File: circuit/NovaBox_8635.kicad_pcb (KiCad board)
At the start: 2 copper layers, 82 x 30 mm, 87 parts, among them P1 MH, P2 MH, P3 MH, P4 MH, P5 USB, Q1 MMBT3904, Q2 IRLML6344, Q3 IRLML6401, Q4 MMBT3904, Q5 MMBT3904, SW1 PIO18, SW2 PIO21, SW3 PIO8, SW4 PIO0, SW5 PIO1, SW6 ON/OFF, U1 MCP6004, U2 CSR8635_MODULE, U3 CSR_DebugSmall, U4 PAM8304, U5 PAM8304, U6 LT1308

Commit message: first draft of PCB; deleted footprints
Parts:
- removed D9: PWR, NovaBox:LED_0805
- removed R5: 1K, NovaBox:R_0805
- moved R1 10.7 mm to (118.9, 63.8)
- moved R3 9.97 mm to (120.7, 57.4), turned to 90 degrees
- moved Q3 9.54 mm to (117.6, 57.9), turned to 0 degrees
- moved Q5 8.93 mm to (115.6, 61.9)
- moved C3 7.71 mm to (116.8, 65.8)
- moved R2 7.70 mm to (114.8, 65.8)
- moved C1 2.03 mm to (110.8, 60.7)
- moved R6 2.03 mm to (110.8, 62.7)
- moved R9 1.13 mm to (110.8, 66.8)
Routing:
- net VR_SHDN: track 5.71 -> 22.7 mm
- net Net-(R9-Pad2): track 134.6 -> 126.0 mm
- net +BATT: track 162.5 -> 168.0 mm
- net +5V: track 129.2 -> 123.9 mm
- net 1V8: track 18.2 -> 14.3 mm
- net Net-(D9-Pad1): track 2.05 -> 0.00 mm
- net Net-(Q3-Pad1): track 5.13 -> 6.81 mm
- net Net-(BT1-Pad2): track 81.1 -> 80.1 mm
- net Net-(D1-Pad3): track 5.81 -> 6.55 mm
- net LED2: track 8.97 -> 9.62 mm

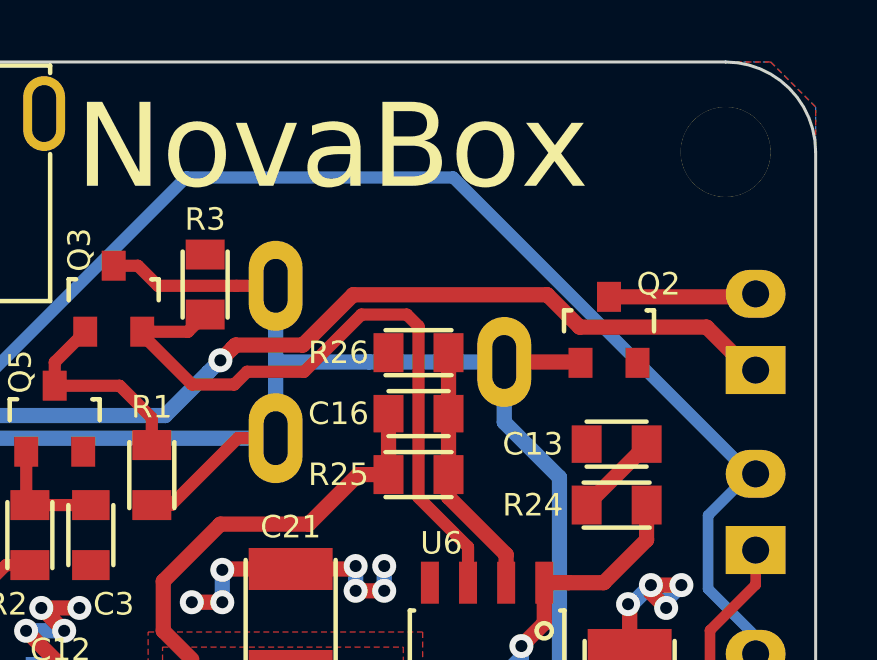
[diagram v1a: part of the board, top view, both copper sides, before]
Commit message: added OSHW; fixed trace over zone; fixed date
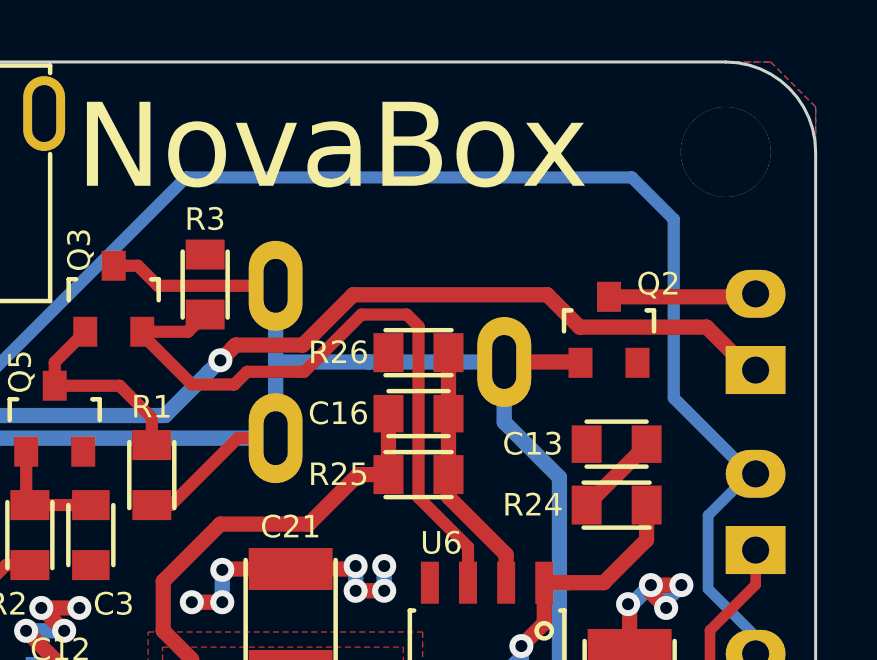
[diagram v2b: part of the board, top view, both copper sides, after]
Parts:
- added G***: OSHW-logo_silkscreen-front_8mm, NovaBox:OSHW_8mm, B.Cu at (68.3, 73.2)
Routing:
- net Net-(R9-Pad2): track 126.0 -> 129.5 mm
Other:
- board text added: "2018.aug.13"
- board text removed: "2017.feb.15"
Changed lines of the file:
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@@
     (thickness 1.6)
     (drawings 21)
-    (tracks 663)
+    (tracks 665)
     (zones 0)
-    (modules 85)
+    (modules 86)
     (nets 69)
   )
@@
   )
   (setup
-    (last_trace_width 0.4064)
+    (last_trace_width 0.2032)
     (user_trace_width 0.254)
     (user_trace_width 0.3048)
@@
     )
   )
+  (module NovaBox:OSHW_8mm (layer B.Cu)
+    (at 68.326 73.152)
+    (fp_text reference G*** (at 0 -4.2418) (layer B.SilkS) hide
+      (effects (font (size 0.36322 0.36322) (thickness 0.07112)) (justify mirror))
+    )
+    (fp_text value OSHW-logo_silkscreen-front_8mm (at 0 4.2418) (layer B.SilkS) hide
+      (effects (font (size 0.36322 0.36322) (thickness 0.07112)) (justify mirror))
+    )
+    (fp_poly (pts (xy -2.42316 -3.59156) (xy -2.38252 -3.57124) (xy -2.28854 -3.51282) (xy -2.15392 -3.42392)
+      (xy -1.99644 -3.31978) (xy -1.83896 -3.21056) (xy -1.70942 -3.1242) (xy -1.61798 -3.06578)
+      (xy -1.57988 -3.04546) (xy -1.55956 -3.05054) (xy -1.48336 -3.08864) (xy -1.37414 -3.14452)
+      (xy -1.31064 -3.17754) (xy -1.21158 -3.22072) (xy -1.16078 -3.23088) (xy -1.15316 -3.21564)
+      (xy -1.11506 -3.13944) (xy -1.05918 -3.00736) (xy -0.98298 -2.83464) (xy -0.89662 -2.63144)
+      (xy -0.80264 -2.413) (xy -0.7112 -2.18948) (xy -0.6223 -1.97612) (xy -0.54356 -1.78562)
+      (xy -0.48006 -1.63068) (xy -0.43942 -1.52146) (xy -0.42418 -1.47574) (xy -0.42926 -1.46558)
+      (xy -0.48006 -1.41732) (xy -0.56642 -1.35128) (xy -0.75692 -1.19634) (xy -0.94234 -0.96266)
+      (xy -1.05664 -0.6985) (xy -1.09474 -0.40386) (xy -1.06172 -0.13208) (xy -0.95504 0.12954)
+      (xy -0.77216 0.36576) (xy -0.55118 0.54102) (xy -0.2921 0.65278) (xy 0 0.68834)
+      (xy 0.2794 0.65786) (xy 0.5461 0.55118) (xy 0.78232 0.37084) (xy 0.88138 0.25654)
+      (xy 1.01854 0.01778) (xy 1.09728 -0.23876) (xy 1.1049 -0.30226) (xy 1.09474 -0.5842)
+      (xy 1.01092 -0.85344) (xy 0.8636 -1.09474) (xy 0.65786 -1.29032) (xy 0.62992 -1.31064)
+      (xy 0.53594 -1.38176) (xy 0.47244 -1.43002) (xy 0.42164 -1.47066) (xy 0.77978 -2.33172)
+      (xy 0.83566 -2.46888) (xy 0.93472 -2.7051) (xy 1.02108 -2.9083) (xy 1.08966 -3.06832)
+      (xy 1.13792 -3.17754) (xy 1.15824 -3.22072) (xy 1.16078 -3.22326) (xy 1.19126 -3.22834)
+      (xy 1.2573 -3.20294) (xy 1.37668 -3.14452) (xy 1.45796 -3.10388) (xy 1.5494 -3.0607)
+      (xy 1.59004 -3.04546) (xy 1.6256 -3.06324) (xy 1.71196 -3.12166) (xy 1.8415 -3.20548)
+      (xy 1.9939 -3.30962) (xy 2.14122 -3.41122) (xy 2.27584 -3.50012) (xy 2.3749 -3.56108)
+      (xy 2.42316 -3.58902) (xy 2.43078 -3.58902) (xy 2.47142 -3.56362) (xy 2.55016 -3.50012)
+      (xy 2.667 -3.38836) (xy 2.8321 -3.2258) (xy 2.8575 -3.2004) (xy 2.99466 -3.0607)
+      (xy 3.10642 -2.94386) (xy 3.18008 -2.86258) (xy 3.20548 -2.82448) (xy 3.18262 -2.77622)
+      (xy 3.11912 -2.6797) (xy 3.03022 -2.54254) (xy 2.921 -2.38252) (xy 2.63652 -1.9685)
+      (xy 2.794 -1.57734) (xy 2.84226 -1.45796) (xy 2.90322 -1.31318) (xy 2.9464 -1.20904)
+      (xy 2.9718 -1.16332) (xy 3.01244 -1.14808) (xy 3.12166 -1.12268) (xy 3.2766 -1.08966)
+      (xy 3.45948 -1.05664) (xy 3.63728 -1.02362) (xy 3.7973 -0.99314) (xy 3.9116 -0.97028)
+      (xy 3.9624 -0.96012) (xy 3.9751 -0.9525) (xy 3.98526 -0.9271) (xy 3.99288 -0.87376)
+      (xy 3.99542 -0.77724) (xy 3.99796 -0.62484) (xy 3.99796 -0.40386) (xy 3.99796 -0.381)
+      (xy 3.99542 -0.17018) (xy 3.99288 -0.00254) (xy 3.9878 0.10668) (xy 3.98018 0.14986)
+      (xy 3.92938 0.16256) (xy 3.81762 0.18542) (xy 3.6576 0.21844) (xy 3.4671 0.254)
+      (xy 3.45694 0.25654) (xy 3.26644 0.2921) (xy 3.10896 0.32512) (xy 2.9972 0.35052)
+      (xy 2.95148 0.36576) (xy 2.94132 0.37846) (xy 2.90322 0.45212) (xy 2.84734 0.56896)
+      (xy 2.78638 0.71374) (xy 2.72288 0.86106) (xy 2.66954 0.99568) (xy 2.63398 1.09474)
+      (xy 2.62382 1.14046) (xy 2.65176 1.18618) (xy 2.7178 1.28524) (xy 2.80924 1.41986)
+      (xy 2.921 1.58242) (xy 2.92862 1.59512) (xy 3.03784 1.75514) (xy 3.12674 1.88976)
+      (xy 3.18516 1.98628) (xy 3.20548 2.02946) (xy 3.20548 2.032) (xy 3.16992 2.08026)
+      (xy 3.08864 2.16916) (xy 2.9718 2.29108) (xy 2.8321 2.43332) (xy 2.78638 2.4765)
+      (xy 2.63144 2.6289) (xy 2.52476 2.72796) (xy 2.45618 2.7813) (xy 2.42316 2.794)
+      (xy 2.42316 2.79146) (xy 2.3749 2.76352) (xy 2.2733 2.69748) (xy 2.13614 2.6035)
+      (xy 1.97358 2.49428) (xy 1.96342 2.48666) (xy 1.8034 2.37744) (xy 1.67132 2.28854)
+      (xy 1.5748 2.22504) (xy 1.53416 2.19964) (xy 1.52654 2.19964) (xy 1.46304 2.21996)
+      (xy 1.34874 2.25806) (xy 1.20904 2.31394) (xy 1.06172 2.37236) (xy 0.9271 2.42824)
+      (xy 0.8255 2.4765) (xy 0.77724 2.5019) (xy 0.77724 2.50444) (xy 0.75946 2.56286)
+      (xy 0.73152 2.68224) (xy 0.6985 2.84734) (xy 0.6604 3.04292) (xy 0.65532 3.0734)
+      (xy 0.61976 3.2639) (xy 0.58928 3.42138) (xy 0.56642 3.5306) (xy 0.55372 3.57632)
+      (xy 0.52832 3.5814) (xy 0.43434 3.58902) (xy 0.2921 3.59156) (xy 0.11938 3.5941)
+      (xy -0.06096 3.59156) (xy -0.23622 3.58902) (xy -0.38862 3.58394) (xy -0.4953 3.57632)
+      (xy -0.54102 3.56616) (xy -0.54356 3.56362) (xy -0.5588 3.5052) (xy -0.5842 3.38582)
+      (xy -0.61976 3.22072) (xy -0.65786 3.0226) (xy -0.66294 2.98958) (xy -0.6985 2.79908)
+      (xy -0.73152 2.64414) (xy -0.75438 2.53492) (xy -0.76708 2.49428) (xy -0.78232 2.48412)
+      (xy -0.86106 2.4511) (xy -0.98806 2.39776) (xy -1.14808 2.33426) (xy -1.51384 2.1844)
+      (xy -1.96088 2.49428) (xy -2.00406 2.52222) (xy -2.16408 2.63144) (xy -2.2987 2.72034)
+      (xy -2.39014 2.77876) (xy -2.42824 2.80162) (xy -2.43078 2.79908) (xy -2.4765 2.76098)
+      (xy -2.5654 2.67716) (xy -2.68732 2.55778) (xy -2.82702 2.41808) (xy -2.93116 2.31394)
+      (xy -3.05562 2.18694) (xy -3.13436 2.10312) (xy -3.17754 2.04724) (xy -3.19278 2.01422)
+      (xy -3.1877 1.9939) (xy -3.15976 1.94818) (xy -3.09372 1.84912) (xy -3.00228 1.71196)
+      (xy -2.89306 1.55448) (xy -2.80162 1.41986) (xy -2.7051 1.27) (xy -2.6416 1.16332)
+      (xy -2.61874 1.10998) (xy -2.62382 1.08712) (xy -2.65684 1.00076) (xy -2.71018 0.86614)
+      (xy -2.77622 0.70866) (xy -2.9337 0.35306) (xy -3.16738 0.30988) (xy -3.30708 0.28194)
+      (xy -3.5052 0.24384) (xy -3.69316 0.20828) (xy -3.9878 0.14986) (xy -3.99796 -0.93218)
+      (xy -3.95224 -0.9525) (xy -3.90906 -0.9652) (xy -3.79984 -0.98806) (xy -3.6449 -1.01854)
+      (xy -3.45948 -1.0541) (xy -3.30454 -1.08458) (xy -3.14452 -1.11252) (xy -3.03276 -1.13538)
+      (xy -2.98196 -1.14554) (xy -2.96926 -1.16332) (xy -2.92862 -1.23952) (xy -2.87274 -1.36144)
+      (xy -2.81178 -1.50876) (xy -2.74828 -1.65862) (xy -2.6924 -1.79832) (xy -2.65176 -1.905)
+      (xy -2.63906 -1.96088) (xy -2.65938 -2.00406) (xy -2.72034 -2.0955) (xy -2.8067 -2.22758)
+      (xy -2.91338 -2.38506) (xy -3.0226 -2.54254) (xy -3.1115 -2.67716) (xy -3.175 -2.77368)
+      (xy -3.2004 -2.81686) (xy -3.1877 -2.84734) (xy -3.12674 -2.92354) (xy -3.00736 -3.04546)
+      (xy -2.8321 -3.22072) (xy -2.80162 -3.24866) (xy -2.66192 -3.38328) (xy -2.54254 -3.4925)
+      (xy -2.46126 -3.56616) (xy -2.42316 -3.59156)) (layer B.SilkS) (width 0.00254))
+  )
   (gr_text https://github.com/nodep/NovaBox (at 99.1235 66.548) (layer B.SilkS)
     (effects (font (size 1.5 1.5) (thickness 0.3)) (justify mirror))
@@
   (gr_arc (start 62 77) (end 62 80) (angle 90) (layer Edge.Cuts) (width 0.1))
   (gr_arc (start 62 53) (end 59 53) (angle 90) (layer Edge.Cuts) (width 0.1))
-  (gr_text 2017.feb.15 (at 88.9 54.2925) (layer B.SilkS)
+  (gr_text 2018.aug.13 (at 88.9 54.2925) (layer B.SilkS)
     (effects (font (size 1.5 1.5) (thickness 0.3)) (justify mirror))
   )
@@
   (segment (start 137.414 67.564) (end 137.414 65.116) (width 0.3556) (layer B.Cu) (net 28))
   (segment (start 137.414 65.116) (end 138.8 63.73) (width 0.3556) (layer B.Cu) (net 28) (status 20))
-  (segment (start 138.8 63.73) (end 139 63.73) (width 0.3556) (layer B.Cu) (net 28) (status 30))
   (segment (start 138.8 69.73) (end 139 69.73) (width 0.4064) (layer B.Cu) (net 28) (status 30))
   (via (at 64.2 51.3) (size 0.8) (drill 0.4) (layers F.Cu B.Cu) (net 28))
@@
   (segment (start 61 72.27) (end 61.2 72.27) (width 0.4064) (layer F.Cu) (net 28) (status 30))
   (segment (start 61 60.27) (end 60.8 60.27) (width 0.4064) (layer B.Cu) (net 28) (status 30))
-  (segment (start 128.918 53.848) (end 120.014982 53.848) (width 0.4064) (layer B.Cu) (net 28))
   (segment (start 120.014982 53.848) (end 113.429981 60.433001) (width 0.4064) (layer B.Cu) (net 28))
-  (segment (start 138.8 63.73) (end 128.918 53.848) (width 0.4064) (layer B.Cu) (net 28))
   (segment (start 113.429981 60.433001) (end 113.029982 60.833) (width 0.4064) (layer B.Cu) (net 28))
   (via (at 113.029982 60.833) (size 0.8) (drill 0.4) (layers F.Cu B.Cu) (net 28))
@@
   (segment (start 113.029982 66.438418) (end 112.6664 66.802) (width 0.4064) (layer F.Cu) (net 28))
   (segment (start 113.029982 60.833) (end 113.029982 66.438418) (width 0.4064) (layer F.Cu) (net 28))
+  (segment (start 120.014982 53.848) (end 134.874 53.848) (width 0.4064) (layer B.Cu) (net 28))
+  (segment (start 134.874 53.848) (end 136.271 55.245) (width 0.4064) (layer B.Cu) (net 28))
+  (segment (start 138.8 63.73) (end 139 63.73) (width 0.4064) (layer B.Cu) (net 28))
+  (segment (start 136.271 61.201) (end 138.8 63.73) (width 0.4064) (layer B.Cu) (net 28))
+  (segment (start 136.271 55.245) (end 136.271 61.201) (width 0.4064) (layer B.Cu) (net 28))
   (segment (start 72.081 65.77) (end 72.081 67.365) (width 0.4064) (layer F.Cu) (net 29) (status 10))
   (segment (start 72.081 67.365) (end 71.8 67.646) (width 0.4064) (layer F.Cu) (net 29))

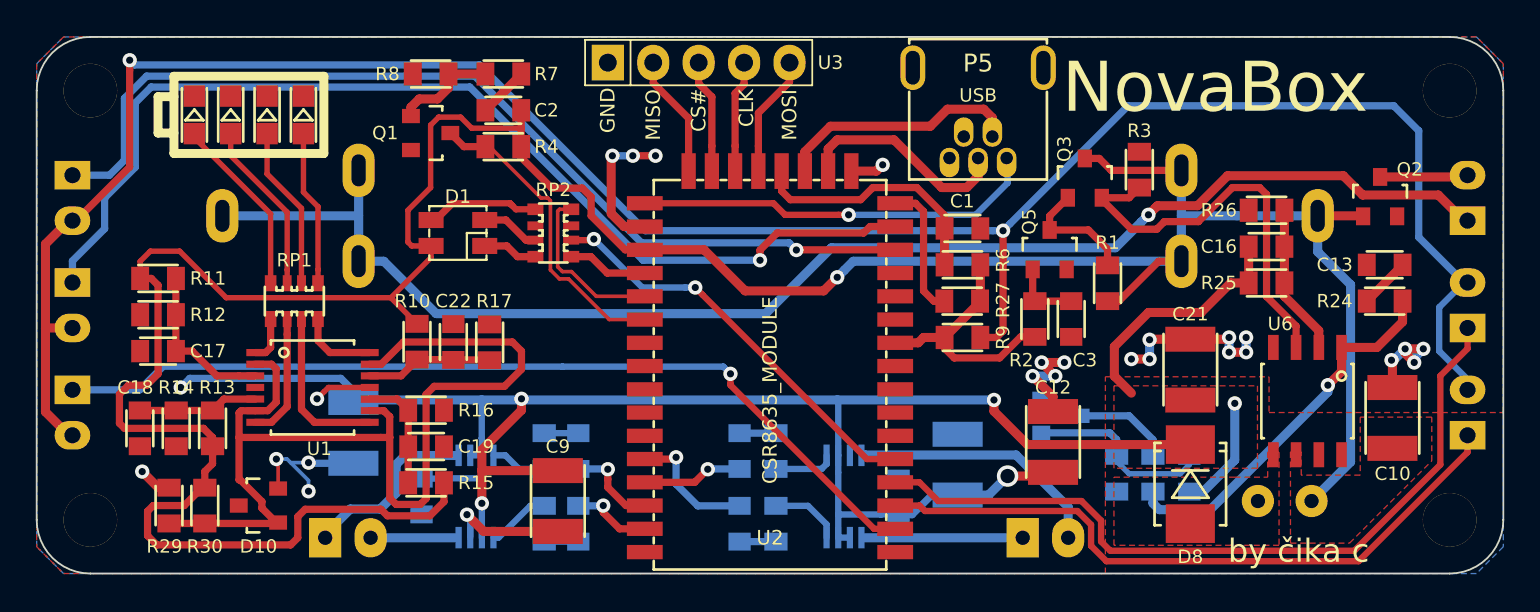
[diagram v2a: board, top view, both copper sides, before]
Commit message: cleaned up the passives around the opeamp
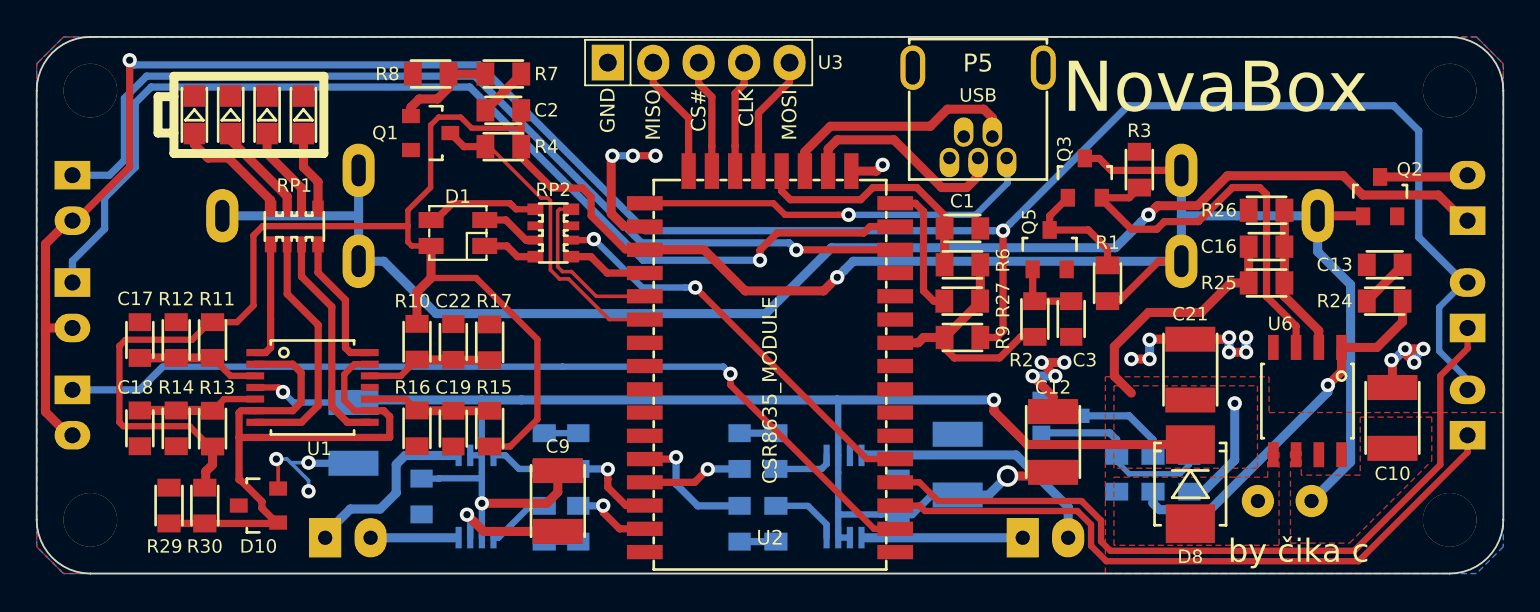
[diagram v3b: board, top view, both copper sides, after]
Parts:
- moved R15 4.67 mm to (84.3, 71.9), turned to 270 degrees
- moved R11 4.60 mm to (68.8, 66.9), turned to 90 degrees
- moved RP1 4.17 mm to (73.4, 60.6)
- moved C19 1.82 mm to (82.3, 71.9), turned to 270 degrees
- moved R12 1.74 mm to (66.8, 66.9), turned to 90 degrees
- moved C17 1.19 mm to (64.8, 66.9), turned to 90 degrees
- moved R16 1.14 mm to (80.3, 71.9), turned to 270 degrees
- turned G*** to 180 degrees
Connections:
- U1 pad 4: (no net) -> +5V
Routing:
- net 2V5: track 57.2 -> 37.0 mm
- net +BATT: track 168.0 -> 155.5 mm
- net +5V: track 123.9 -> 113.6 mm, vias 6 -> 5
- net Net-(RP1-Pad2): track 7.05 -> 13.6 mm
- net GND: track 51.0 -> 45.9 mm, vias 25 -> 23
- net Net-(D7-Pad2): track 8.70 -> 4.53 mm
- net Net-(D6-Pad2): track 9.16 -> 4.99 mm
- net Net-(D5-Pad2): track 9.67 -> 5.50 mm
- net Net-(RP1-Pad1): track 2.57 -> 6.75 mm
- net Net-(D4-Pad2): track 10.1 -> 6.62 mm
- net Net-(RP1-Pad4): track 4.38 -> 7.88 mm
- net Net-(RP1-Pad3): track 9.17 -> 12.3 mm
- net Net-(C17-Pad1): track 9.38 -> 6.87 mm
- net Net-(C19-Pad1): track 6.47 -> 6.98 mm

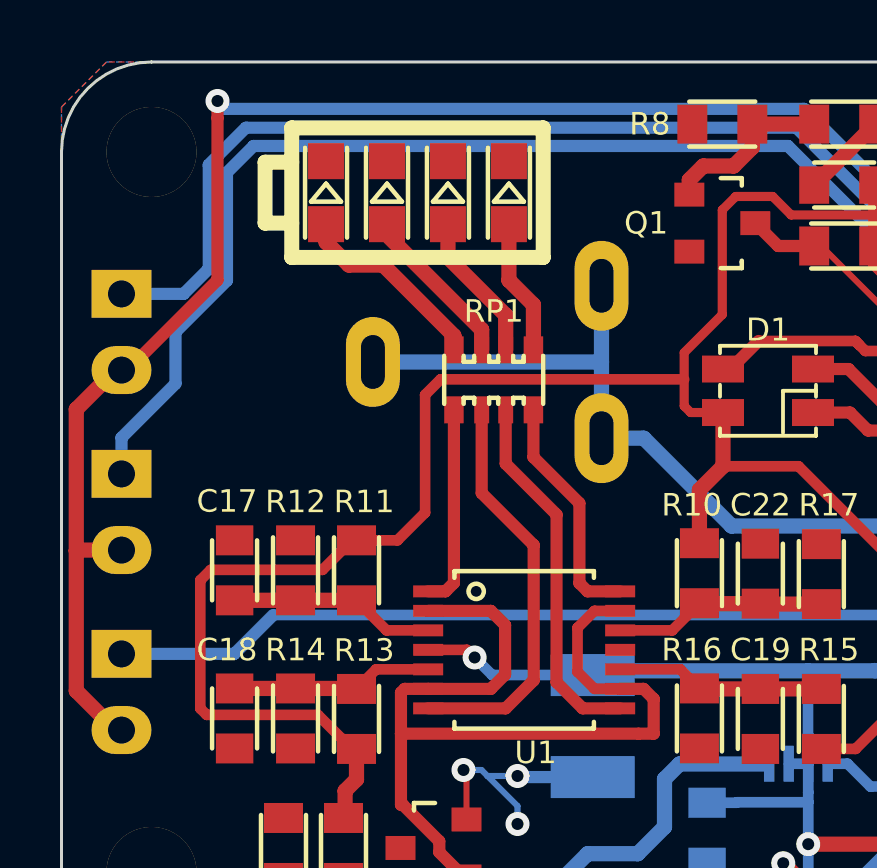
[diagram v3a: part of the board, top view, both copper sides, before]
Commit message: moved battery leds
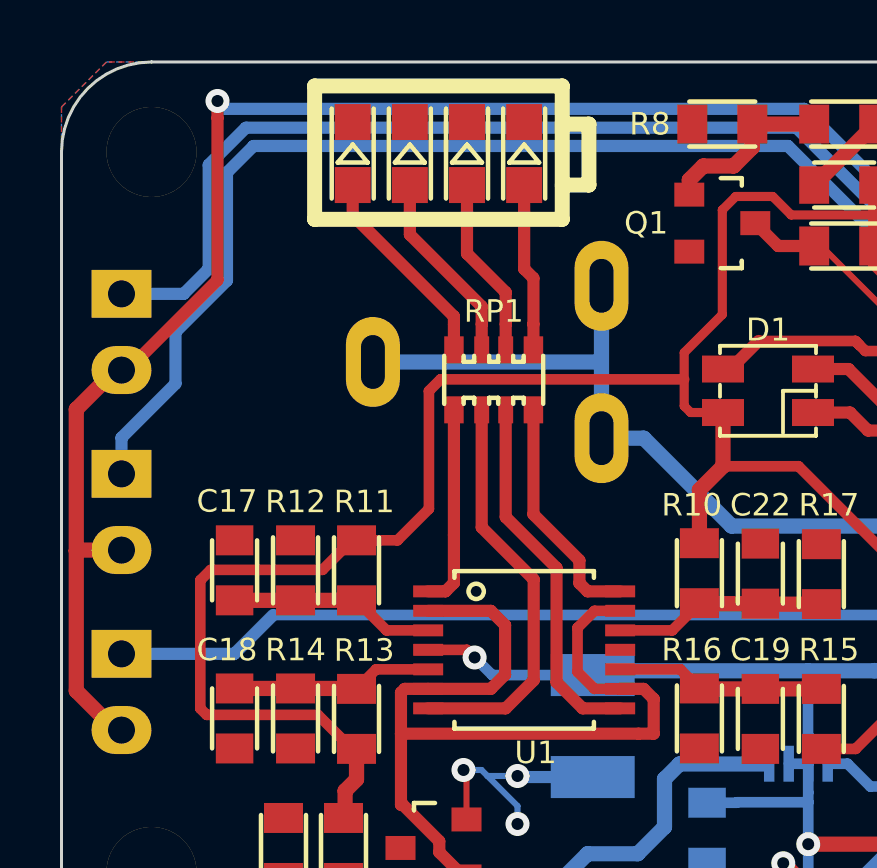
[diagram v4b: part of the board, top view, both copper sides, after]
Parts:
- moved D4 1.58 mm to (68.7, 53.1)
- moved D5 1.51 mm to (70.6, 53.1)
- moved D6 1.45 mm to (72.5, 53.1)
- moved D7 1.40 mm to (74.4, 53.1)
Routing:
- net Net-(D7-Pad2): track 4.53 -> 5.62 mm
- net Net-(D6-Pad2): track 4.99 -> 6.03 mm
- net Net-(D5-Pad2): track 5.50 -> 6.48 mm
